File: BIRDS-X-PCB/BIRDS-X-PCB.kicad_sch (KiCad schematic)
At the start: 1 part, among them J1 Conn_02x25_Odd_Even_MountingP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

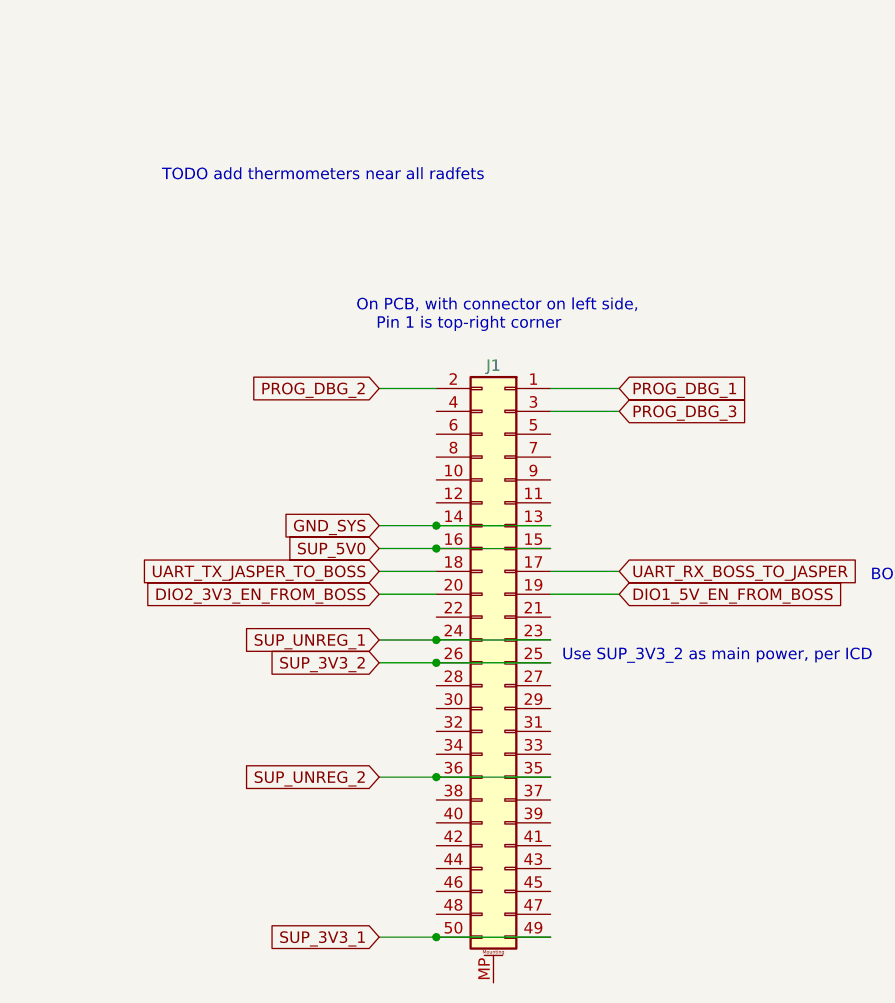
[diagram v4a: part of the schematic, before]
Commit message: Add BOM and footprints
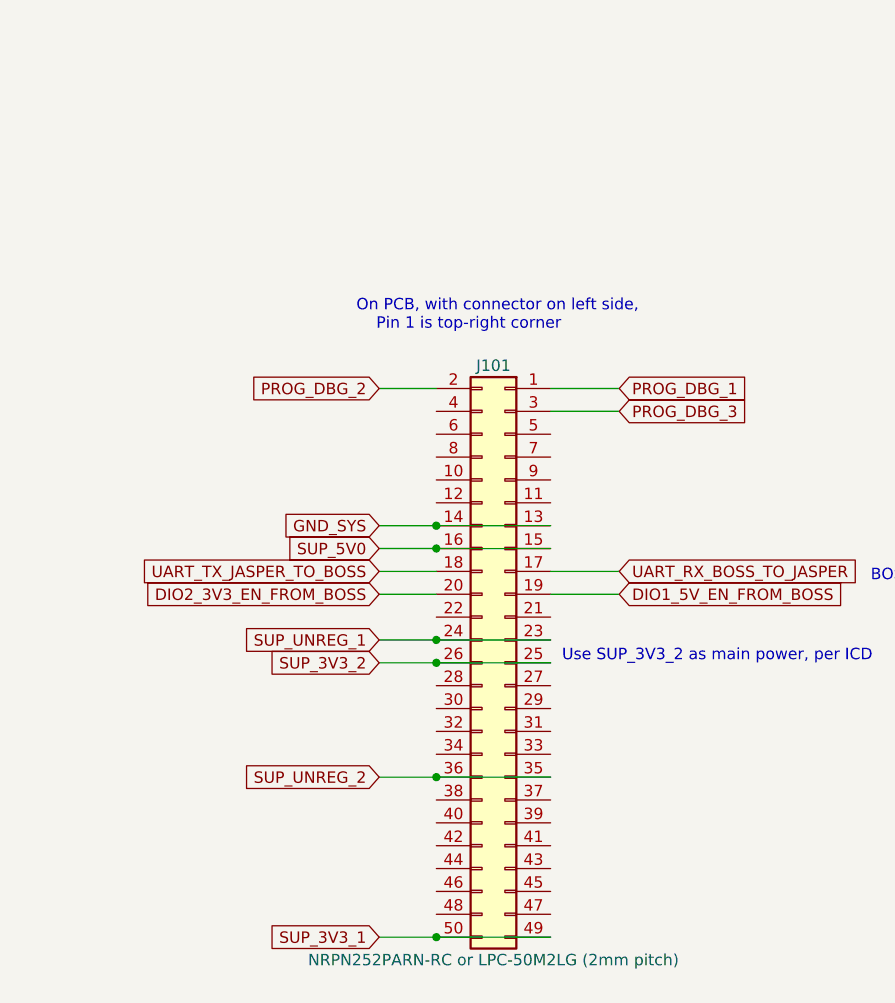
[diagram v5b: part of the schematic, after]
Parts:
- J101: renamed from J1; value Conn_02x25_Odd_Even_MountingPin -> NRPN252PARN-RC or LPC-50M2LG (2mm pitch); symbol Connector_Generic_MountingPin:Conn_02x25_Odd_Even_MountingPin -> Connector_Generic:Conn_02x25_Odd_Even
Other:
- note removed: "TODO add thermometers near all radfets"
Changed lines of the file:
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@@
-    (effects (font (size 1.27 1.27)) (justify left bottom))
-  )
-  (text "TODO add thermometers near all radfets" (at 151.13 64.77 0)
     (effects (font (size 1.27 1.27)) (justify left bottom))
   )
@@
     )
   )
-  (symbol (lib_id "Connector_Generic_MountingPin:Conn_02x25_Odd_Even_MountingPin") (at 189.23 118.11 0) (mirror y) (unit 1)
+  (symbol (lib_id "Connector_Generic:Conn_02x25_Odd_Even") (at 189.23 118.11 0) (mirror y) (unit 1)
     (in_bom yes) (on_board yes) (dnp no)
-    (property "Reference" "J1" (at 187.96 85.09 0)
+    (property "Reference" "J101" (at 187.96 85.09 0)
       (effects (font (size 1.27 1.27)))
     )
-    (property "Value" "Conn_02x25_Odd_Even_MountingPin" (at 187.96 85.09 0)
-      (effects (font (size 1.27 1.27)) hide)
+    (property "Value" "NRPN252PARN-RC or LPC-50M2LG (2mm pitch)" (at 187.96 151.13 0)
+      (effects (font (size 1.27 1.27)))
     )
     (property "Footprint" "" (at 189.23 118.11 0)
@@
     (pin "8")
     (pin "9")
-    (pin "MP")
     (instances
       (project "BIRDS-X-PCB"
         (path "/c2796b15-795a-4d6e-ad4b-0ba87ded4bc9"
-          (reference "J1") (unit 1)
+          (reference "J101") (unit 1)
         )
       )

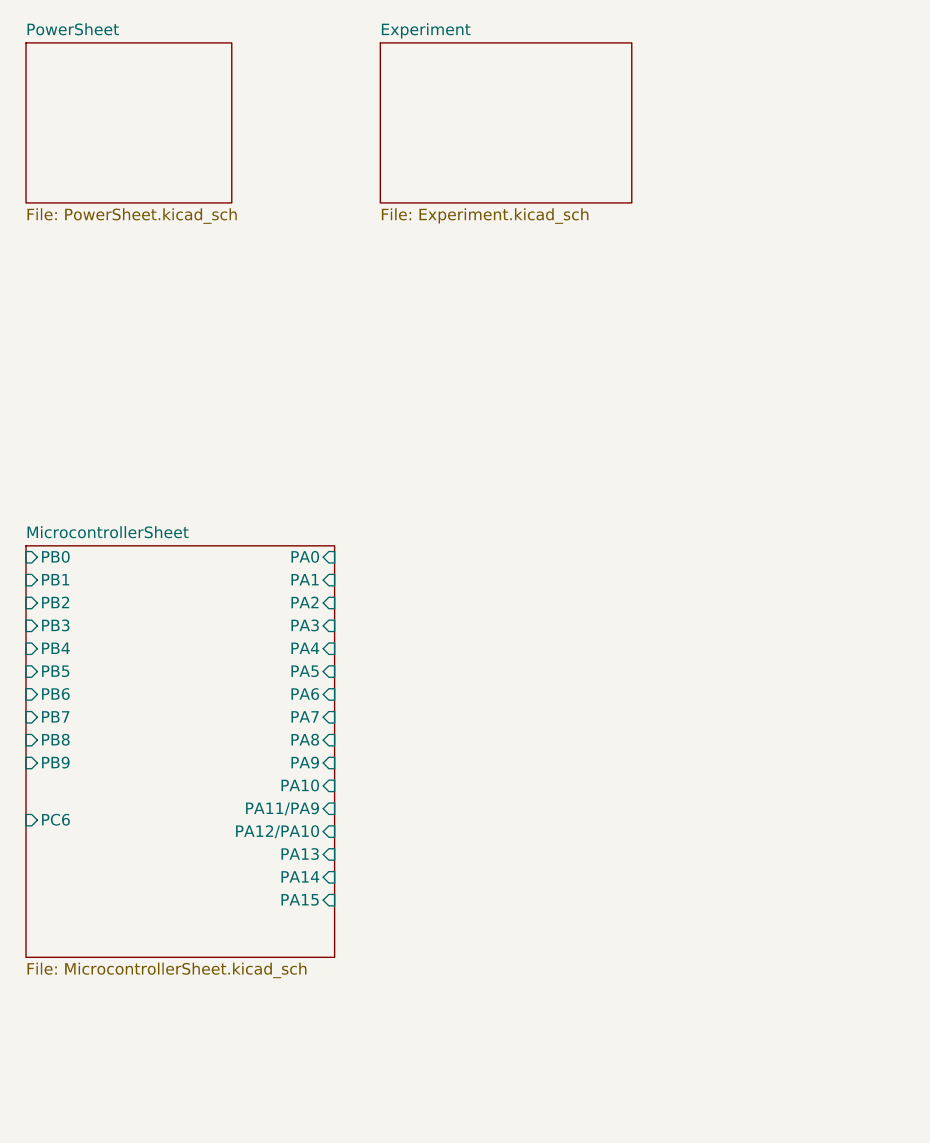
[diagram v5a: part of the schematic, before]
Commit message: Completed MCU & Experiment Circuit
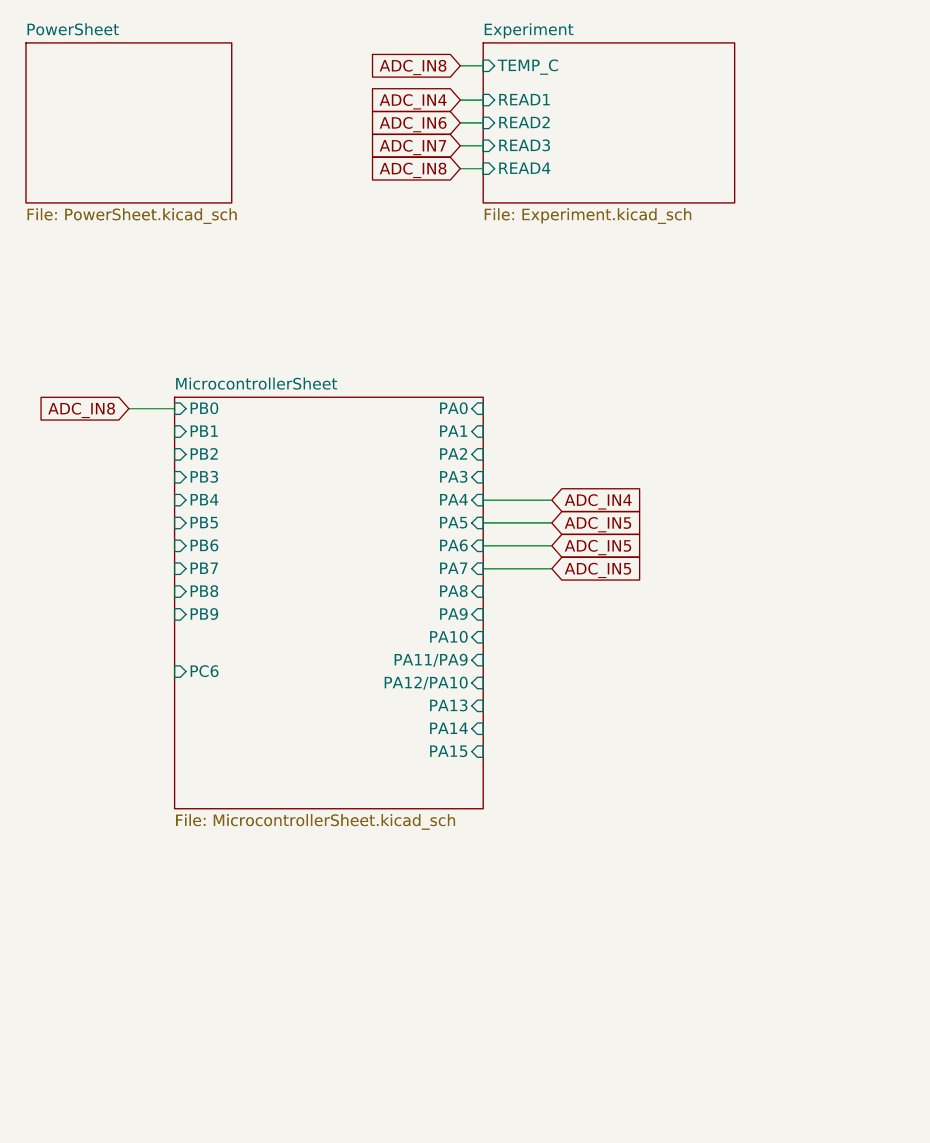
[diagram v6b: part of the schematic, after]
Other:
- sheet Experiment ports: added READ1, READ2, READ3, READ4, TEMP_C; removed none

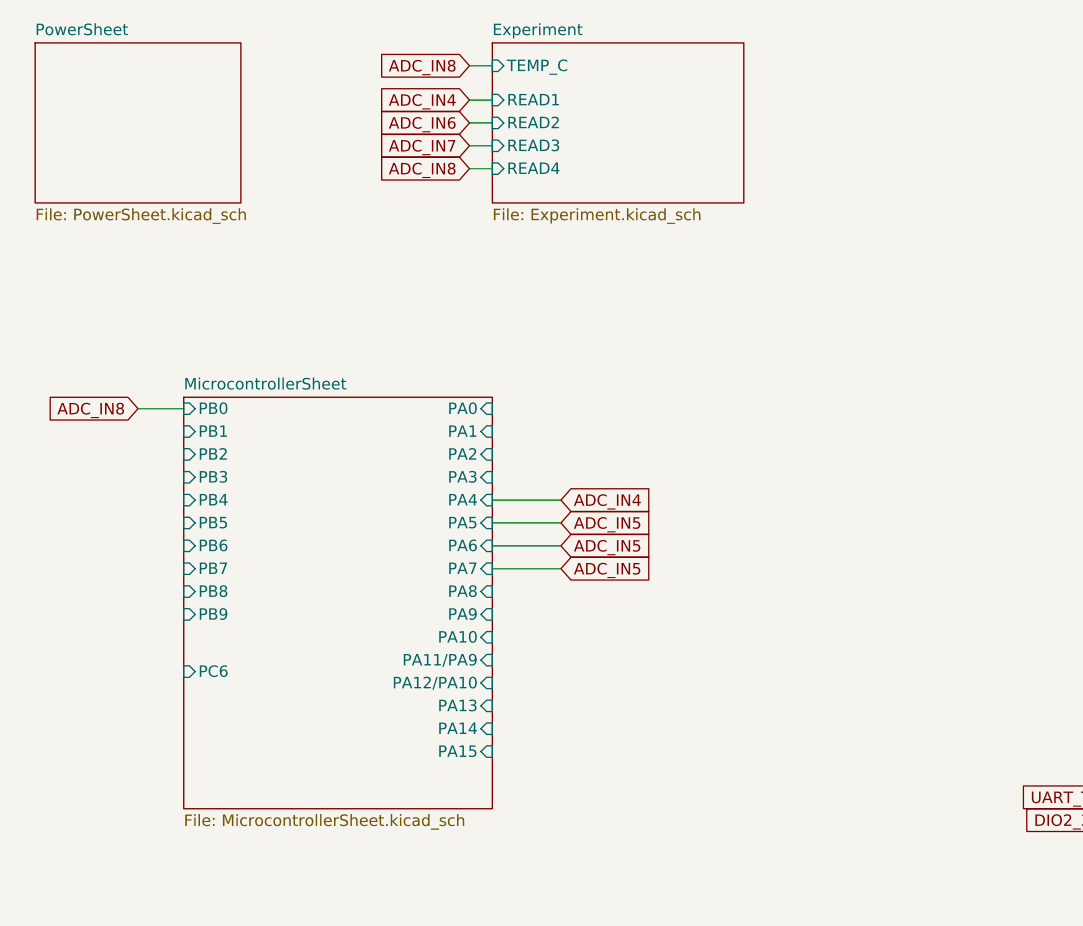
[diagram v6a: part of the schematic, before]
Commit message: Added RFET enabling connections
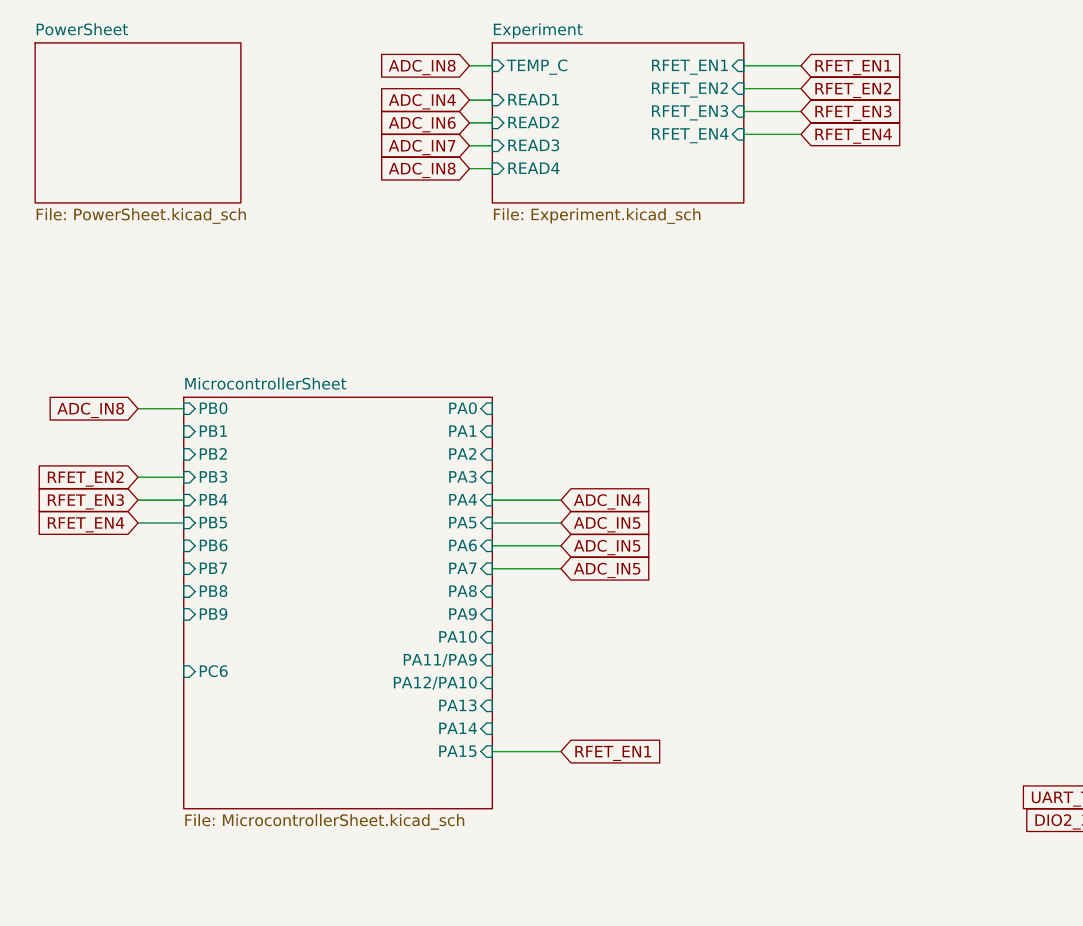
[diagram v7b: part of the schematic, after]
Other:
- sheet Experiment ports: added RFET_EN1, RFET_EN2, RFET_EN3, RFET_EN4; removed none
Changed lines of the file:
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@@
+    (stroke (width 0) (type default))
+  )
+  (wire (pts (xy 90.17 102.87) (xy 97.79 102.87))
     (stroke (width 0) (type default))
   )
@@
     (stroke (width 0) (type default))
   )
+  (wire (pts (xy 118.11 26.67) (xy 124.46 26.67))
+    (stroke (width 0) (type default))
+  )
   (wire (pts (xy 194.31 90.17) (xy 201.93 90.17))
     (stroke (width 0) (type default))
@@
     (stroke (width 0) (type default))
   )
+  (wire (pts (xy 50.8 74.93) (xy 55.88 74.93))
+    (stroke (width 0) (type default))
+  )
   (wire (pts (xy 87.63 33.02) (xy 90.17 33.02))
     (stroke (width 0) (type default))
@@
     (stroke (width 0) (type default))
   )
+  (wire (pts (xy 50.8 72.39) (xy 55.88 72.39))
+    (stroke (width 0) (type default))
+  )
   (wire (pts (xy 181.61 130.81) (xy 194.31 130.81))
     (stroke (width 0) (type default))
@@
     (stroke (width 0) (type default))
   )
+  (wire (pts (xy 118.11 34.29) (xy 124.46 34.29))
+    (stroke (width 0) (type default))
+  )
   (wire (pts (xy 181.61 102.87) (xy 194.31 102.87))
     (stroke (width 0) (type default))
@@
     (stroke (width 0) (type default))
   )
+  (wire (pts (xy 118.11 31.75) (xy 124.46 31.75))
+    (stroke (width 0) (type default))
+  )
   (wire (pts (xy 194.31 107.95) (xy 201.93 107.95))
     (stroke (width 0) (type default))
   )
+  (wire (pts (xy 118.11 29.21) (xy 124.46 29.21))
+    (stroke (width 0) (type default))
+  )
   (wire (pts (xy 90.17 74.93) (xy 97.79 74.93))
     (stroke (width 0) (type default))
@@
   )
   (wire (pts (xy 194.31 110.49) (xy 201.93 110.49))
+    (stroke (width 0) (type default))
+  )
+  (wire (pts (xy 50.8 77.47) (xy 55.88 77.47))
     (stroke (width 0) (type default))
   )
@@
     (effects (font (size 1.27 1.27)) (justify left bottom))
   )
+  (global_label "RFET_EN2" (shape input) (at 50.8 72.39 180) (fields_autoplaced)
+    (effects (font (size 1.27 1.27)) (justify right))
+    (property "Intersheetrefs" "${INTERSHEET_REFS}" (at 38.7624 72.39 0)
+      (effects (font (size 1.27 1.27)) (justify right) hide)
+    )
+  )
   (global_label "ADC_IN6" (shape input) (at 87.63 33.02 180) (fields_autoplaced)
     (effects (font (size 1.27 1.27)) (justify right))
@@
     )
   )
+  (global_label "RFET_EN3" (shape input) (at 124.46 31.75 0) (fields_autoplaced)
+    (effects (font (size 1.27 1.27)) (justify left))
+    (property "Intersheetrefs" "${INTERSHEET_REFS}" (at 136.4976 31.75 0)
+      (effects (font (size 1.27 1.27)) (justify left) hide)
+    )
+  )
   (global_label "ADC_IN5" (shape input) (at 97.79 77.47 0) (fields_autoplaced)
     (effects (font (size 1.27 1.27)) (justify left))
@@
     )
   )
+  (global_label "RFET_EN3" (shape input) (at 50.8 74.93 180) (fields_autoplaced)
+    (effects (font (size 1.27 1.27)) (justify right))
+    (property "Intersheetrefs" "${INTERSHEET_REFS}" (at 38.7624 74.93 0)
+      (effects (font (size 1.27 1.27)) (justify right) hide)
+    )
+  )
   (global_label "ADC_IN8" (shape input) (at 50.8 64.77 180) (fields_autoplaced)
     (effects (font (size 1.27 1.27)) (justify right))
@@
     )
   )
+  (global_label "RFET_EN1" (shape input) (at 97.79 102.87 0) (fields_autoplaced)
+    (effects (font (size 1.27 1.27)) (justify left))
+    (property "Intersheetrefs" "${INTERSHEET_REFS}" (at 109.8276 102.87 0)
+      (effects (font (size 1.27 1.27)) (justify left) hide)
+    )
+  )
   (global_label "ADC_IN5" (shape input) (at 97.79 82.55 0) (fields_autoplaced)
     (effects (font (size 1.27 1.27)) (justify left))
@@
     )
   )
+  (global_label "RFET_EN2" (shape input) (at 124.46 29.21 0) (fields_autoplaced)
+    (effects (font (size 1.27 1.27)) (justify left))
+    (property "Intersheetrefs" "${INTERSHEET_REFS}" (at 136.4976 29.21 0)
+      (effects (font (size 1.27 1.27)) (justify left) hide)
+    )
+  )
+  (global_label "RFET_EN1" (shape input) (at 124.46 26.67 0) (fields_autoplaced)
+    (effects (font (size 1.27 1.27)) (justify left))
+    (property "Intersheetrefs" "${INTERSHEET_REFS}" (at 136.4976 26.67 0)
+      (effects (font (size 1.27 1.27)) (justify left) hide)
+    )
+  )
+  (global_label "RFET_EN4" (shape input) (at 124.46 34.29 0) (fields_autoplaced)
+    (effects (font (size 1.27 1.27)) (justify left))
+    (property "Intersheetrefs" "${INTERSHEET_REFS}" (at 136.4976 34.29 0)
+      (effects (font (size 1.27 1.27)) (justify left) hide)
+    )
+  )
   (global_label "DIO2_3V3_EN_FROM_BOSS" (shape input) (at 175.26 110.49 180) (fields_autoplaced)
     (effects (font (size 1.27 1.27)) (justify right))
     (property "Intersheetrefs" "${INTERSHEET_REFS}" (at 147.9219 110.49 0)
+      (effects (font (size 1.27 1.27)) (justify right) hide)
+    )
+  )
+  (global_label "RFET_EN4" (shape input) (at 50.8 77.47 180) (fields_autoplaced)
+    (effects (font (size 1.27 1.27)) (justify right))
+    (property "Intersheetrefs" "${INTERSHEET_REFS}" (at 38.7624 77.47 0)
       (effects (font (size 1.27 1.27)) (justify right) hide)
     )
@@
       (effects (font (size 1.27 1.27)) (justify left))
     )
+    (pin "RFET_EN3" input (at 118.11 31.75 0)
+      (effects (font (size 1.27 1.27)) (justify right))
+    )
+    (pin "RFET_EN4" input (at 118.11 34.29 0)
+      (effects (font (size 1.27 1.27)) (justify right))
+    )
+    (pin "RFET_EN2" input (at 118.11 29.21 0)
+      (effects (font (size 1.27 1.27)) (justify right))
+    )
+    (pin "RFET_EN1" input (at 118.11 26.67 0)
+      (effects (font (size 1.27 1.27)) (justify right))
+    )
     (instances
